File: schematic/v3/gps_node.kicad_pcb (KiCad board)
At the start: 2 copper layers, 48 x 75 mm, 86 parts, among them IC1 MCP73831/2, J1 Mounting Hole, J11 AVR ICSP, J12 UART RF, J13 LIPO_BAT, J15 UART GPS, J16 FW_UPDATE, J17 u.FL connector, J2 Mounting Hole, J3 Mounting Hole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

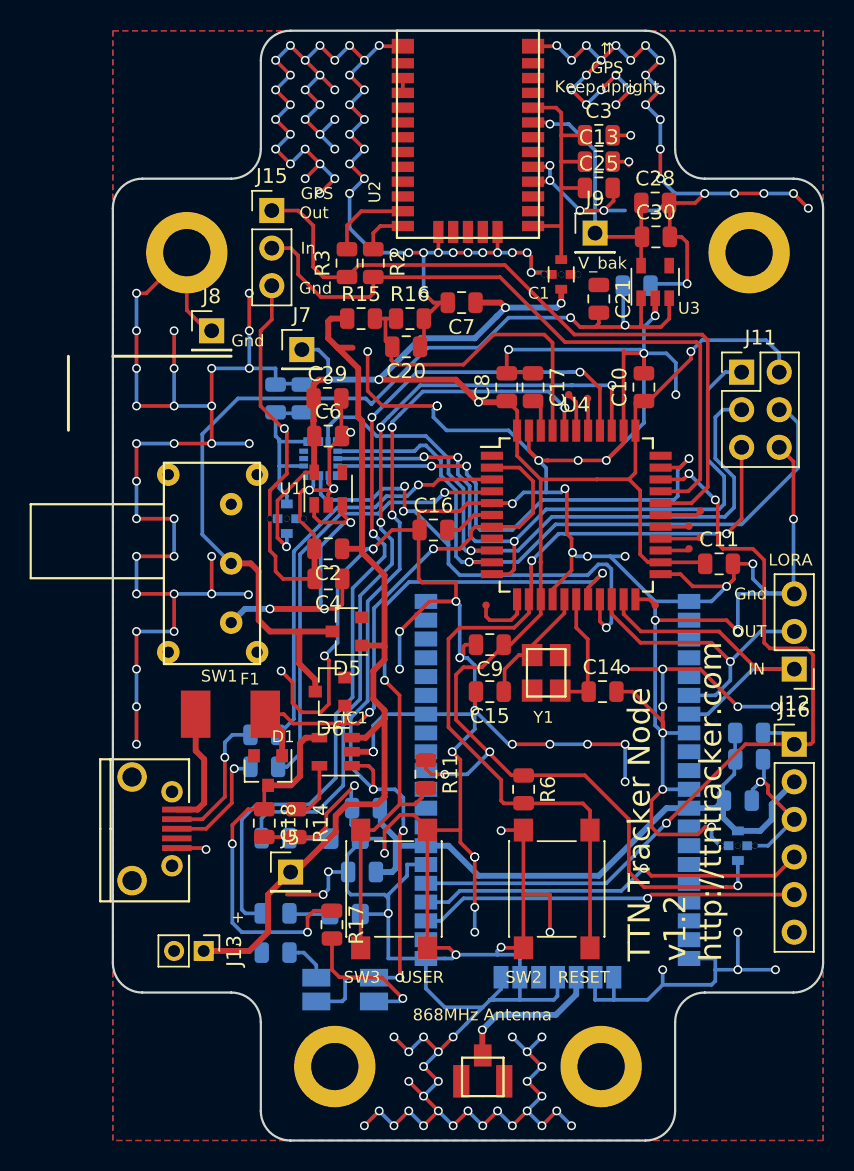
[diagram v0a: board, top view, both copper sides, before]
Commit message: Updated layout
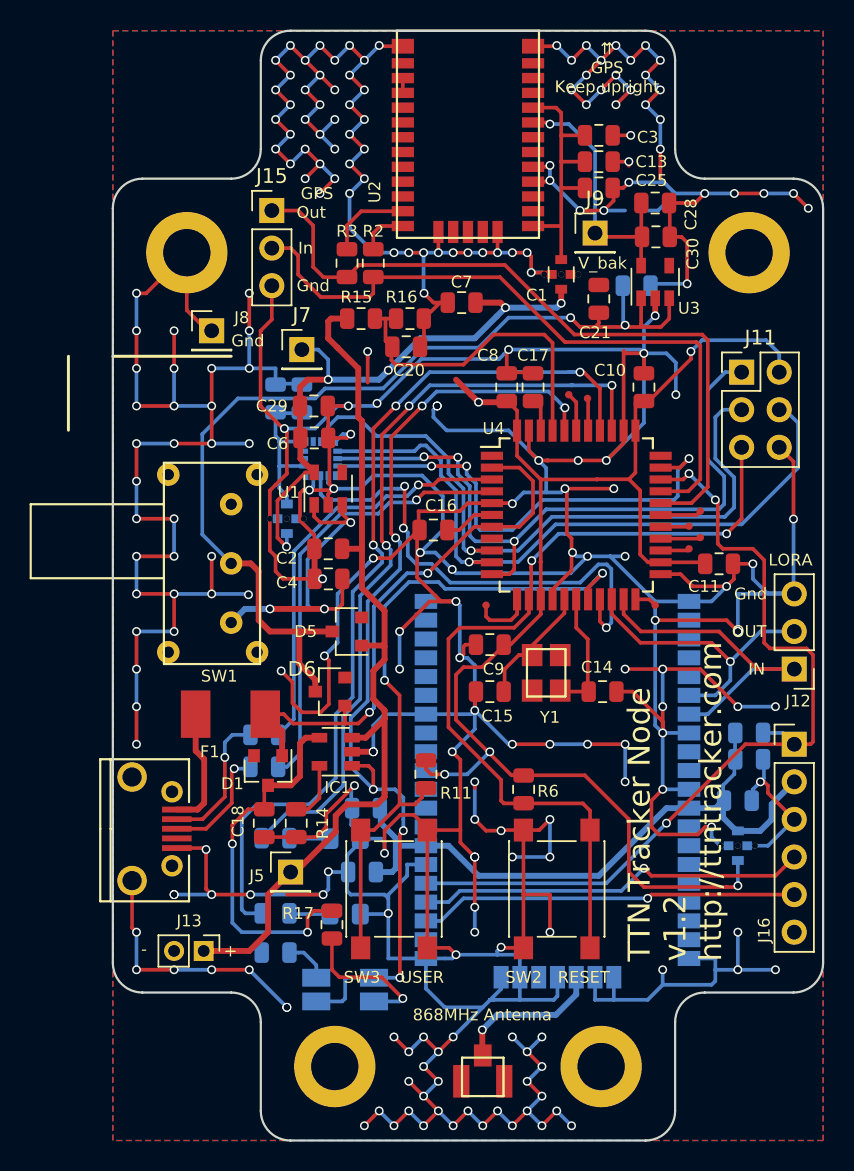
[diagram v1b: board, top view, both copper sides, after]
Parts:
- moved C29 1.05 mm to (113.6, 86.4)
- moved C6 0.95 mm to (113.6, 88.5)
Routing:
- net GND: track 735.1 -> 821.9 mm, vias 211 -> 233
- net V_3.3: track 141.9 -> 137.9 mm
- net /Microcontroller/LED1: track 53.8 -> 52.5 mm
- net /power/V3.3_SUPPLY: track 21.6 -> 22.9 mm
- net /Microcontroller/BUTTON_1: track 45.4 -> 46.6 mm
- net V_BATT: track 61.6 -> 60.6 mm
- net /Microcontroller/LED0: track 61.9 -> 61.2 mm
- net /Microcontroller/ACCEL_INT: track 33.0 -> 33.7 mm
